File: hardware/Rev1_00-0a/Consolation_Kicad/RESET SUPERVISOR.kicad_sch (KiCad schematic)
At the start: 28 parts, among them Q7 SSM3K56FS,LF, Q8 SSM3K56FS,LF, Q9 SSM3K56FS,LF, U30 STM6710DWB6F, U31 SN74LVC1G125DBVR, U32 SN74HCS365QPWRQ1

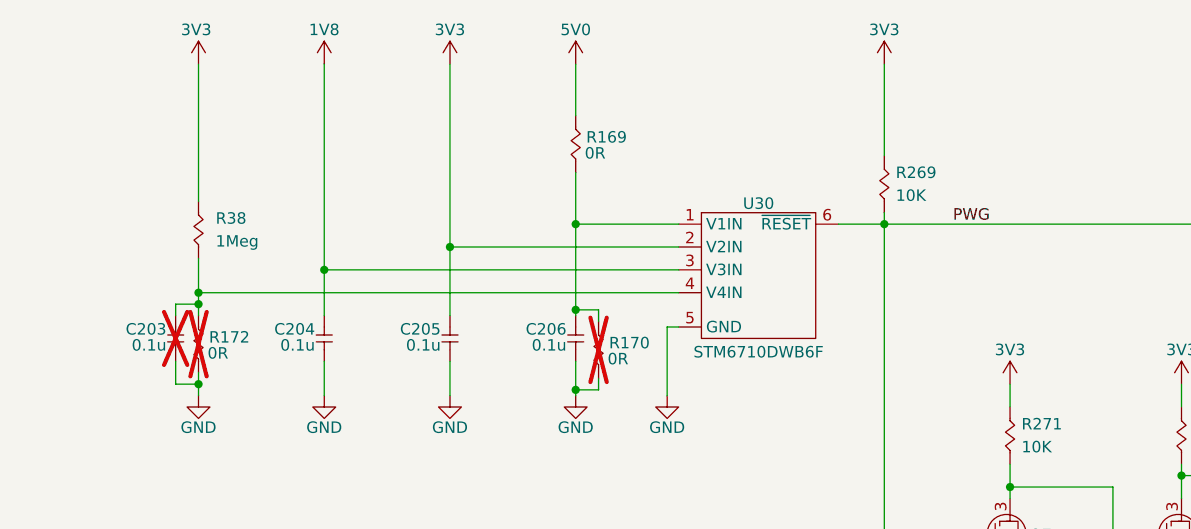
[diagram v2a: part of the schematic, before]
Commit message: Component preliminary placement
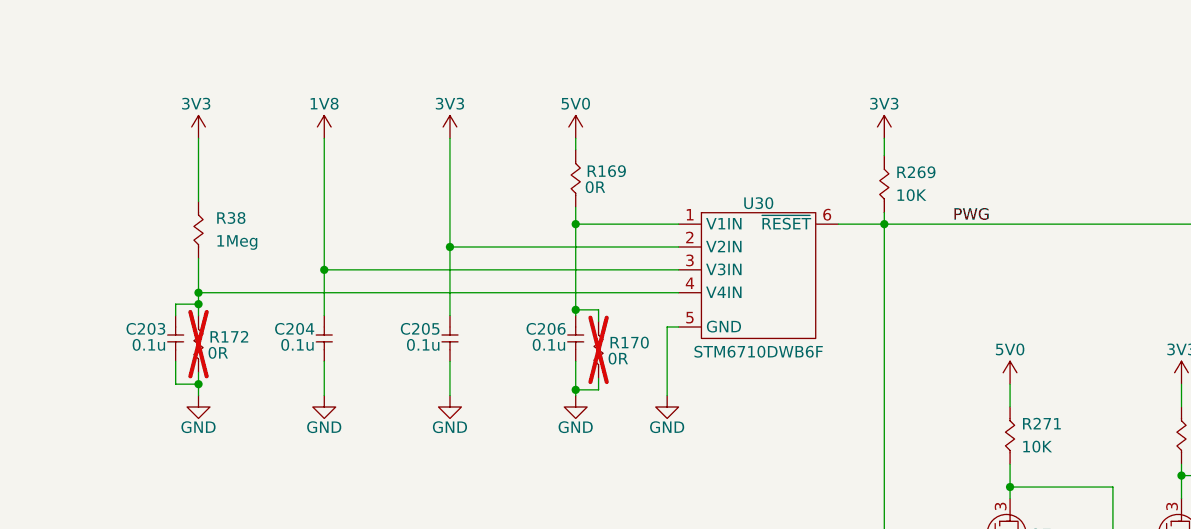
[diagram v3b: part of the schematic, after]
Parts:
- C203: now fitted
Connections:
- net 3V3: no longer R271.2
- net 5V0: now also R271.2
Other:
- moved on the sheet: R169
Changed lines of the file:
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@@
 	)
 	(junction
-		(at 78.105 64.77)
-		(diameter 0)
-		(color 0 0 0 0)
-	)
-	(junction
 		(at 209.55 107.95)
 		(diameter 0)
@@
 	)
 	(junction
-		(at 92.075 62.23)
+		(at 64.135 67.31)
 		(diameter 0)
 		(color 0 0 0 0)
@@
 	)
 	(junction
-		(at 64.135 67.31)
+		(at 78.105 64.77)
+		(diameter 0)
+		(color 0 0 0 0)
+	)
+	(junction
+		(at 92.075 62.23)
 		(diameter 0)
 		(color 0 0 0 0)
@@
 	(wire
 		(pts
-			(xy 50.165 44.45) (xy 50.165 59.69)
+			(xy 50.165 52.705) (xy 50.165 59.69)
 		)
 		(stroke
@@
 	(wire
 		(pts
-			(xy 78.105 44.45) (xy 78.105 64.77)
+			(xy 78.105 52.705) (xy 78.105 64.77)
 		)
 		(stroke
@@
 	(wire
 		(pts
-			(xy 92.075 56.515) (xy 92.075 62.23)
+			(xy 92.075 60.325) (xy 92.075 62.23)
 		)
 		(stroke
@@
 	(wire
 		(pts
-			(xy 126.365 44.45) (xy 126.365 54.61)
+			(xy 126.365 52.705) (xy 126.365 54.61)
 		)
 		(stroke
@@
 	(wire
 		(pts
+			(xy 64.135 67.31) (xy 64.135 72.39)
+		)
+		(stroke
+			(width 0)
+			(type default)
+		)
+	)
+	(wire
+		(pts
 			(xy 207.645 100.33) (xy 216.535 100.33)
 		)
@@
 	(wire
 		(pts
-			(xy 92.075 44.45) (xy 92.075 50.165)
+			(xy 92.075 52.705) (xy 92.075 53.975)
 		)
 		(stroke
@@
 	(wire
 		(pts
-			(xy 64.135 67.31) (xy 64.135 72.39)
-		)
-		(stroke
-			(width 0)
-			(type default)
-		)
-	)
-	(wire
-		(pts
 			(xy 235.585 62.23) (xy 235.585 63.5)
 		)
@@
 	(wire
 		(pts
-			(xy 64.135 44.45) (xy 64.135 67.31)
+			(xy 64.135 52.705) (xy 64.135 67.31)
 		)
 		(stroke
@@
 	(symbol
 		(lib_id "KiCad_Pwr_Symbols:+1V8")
-		(at 50.165 44.45 0)
+		(at 50.165 52.705 0)
 		(unit 1)
 		(body_style 1)
@@
 		(dnp no)
 		(property "Reference" "#PWR0300"
-			(at 50.165 48.26 0)
+			(at 50.165 56.515 0)
 			(hide yes)
 			(show_name no)
@@
 		)
 		(property "Value" "3V3"
-			(at 49.911 40.64 0)
+			(at 49.911 48.895 0)
 			(show_name no)
 			(do_not_autoplace no)
@@
 		)
 		(property "Footprint" ""
-			(at 50.165 44.45 0)
+			(at 50.165 52.705 0)
 			(hide yes)
 			(show_name no)
@@
 		)
 		(property "Datasheet" ""
-			(at 50.165 44.45 0)
+			(at 50.165 52.705 0)
 			(hide yes)
 			(show_name no)
@@
 		)
 		(property "Description" "Power symbol creates a global label with name \"+1V8\""
-			(at 50.165 44.45 0)
+			(at 50.165 52.705 0)
 			(hide yes)
 			(show_name no)
@@
 	(symbol
 		(lib_id "KiCad_Pwr_Symbols:+1V8")
-		(at 78.105 44.45 0)
+		(at 78.105 52.705 0)
 		(unit 1)
 		(body_style 1)
@@
 		(dnp no)
 		(property "Reference" "#PWR0304"
-			(at 78.105 48.26 0)
+			(at 78.105 56.515 0)
 			(hide yes)
 			(show_name no)
@@
 		)
 		(property "Value" "3V3"
-			(at 78.105 40.64 0)
+			(at 78.105 48.895 0)
 			(show_name no)
 			(do_not_autoplace no)
@@
 		)
 		(property "Footprint" ""
-			(at 78.105 44.45 0)
+			(at 78.105 52.705 0)
 			(hide yes)
 			(show_name no)
@@
 		)
 		(property "Datasheet" ""
-			(at 78.105 44.45 0)
+			(at 78.105 52.705 0)
 			(hide yes)
 			(show_name no)
@@
 		)
 		(property "Description" "Power symbol creates a global label with name \"+1V8\""
-			(at 78.105 44.45 0)
+			(at 78.105 52.705 0)
 			(hide yes)
 			(show_name no)
@@
 			)
 		)
-		(property "Value" "3V3"
+		(property "Value" "5V0"
 			(at 140.335 76.2 0)
 			(show_name no)
@@
 	(symbol
 		(lib_id "KicadCompDb:Resistors/RES_SMT_00001")
-		(at 92.075 55.245 90)
+		(at 92.075 59.055 90)
 		(unit 1)
 		(body_style 1)
@@
 		(dnp no)
 		(property "Reference" "R169"
-			(at 95.504 52.578 90)
+			(at 95.504 56.388 90)
 			(show_name no)
 			(do_not_autoplace no)
@@
 		)
 		(property "Value" "0R"
-			(at 94.234 54.356 90)
+			(at 94.234 58.166 90)
 			(show_name no)
 			(do_not_autoplace no)
@@
 		)
 		(property "Footprint" "footprint:RES_0402"
-			(at 114.173 54.737 0)
+			(at 114.173 58.547 0)
 			(hide yes)
 			(show_name no)
@@
 		)
 		(property "Datasheet" "https://www.yageogroup.com/content/datasheet/asset/file/PYU-RC_GROUP_51_ROHS_L"
-			(at 92.075 55.245 0)
+			(at 92.075 59.055 0)
 			(hide yes)
 			(show_name no)
@@
 		)
 		(property "Description" "RES 0 OHM JUMPER 1/16W 0402"
-			(at 101.981 53.467 0)
+			(at 101.981 57.277 0)
 			(hide yes)
 			(show_name no)
@@
 		)
 		(property "Tolerance" "1%"
-			(at 112.395 54.991 0)
+			(at 112.395 58.801 0)
 			(hide yes)
 			(show_name no)
@@
 		)
 		(property "Power" "1/16W"
-			(at 106.299 54.991 0)
+			(at 106.299 58.801 0)
 			(hide yes)
 			(show_name no)
@@
 		)
 		(property "Package" "0402"
-			(at 108.331 55.245 0)
+			(at 108.331 59.055 0)
 			(hide yes)
 			(show_name no)
@@
 		)
 		(property "Manufacturer" "YAGEO"
-			(at 110.363 54.991 0)
+			(at 110.363 58.801 0)
 			(hide yes)
 			(show_name no)
@@
 		)
 		(property "Manufacturer Part Number" "RC0402FR-071KL"
-			(at 99.949 54.991 0)
+			(at 99.949 58.801 0)
 			(hide yes)
 			(show_name no)
@@
 		)
 		(property "Distributor" "DigiKey"
-			(at 97.917 55.245 0)
+			(at 97.917 59.055 0)
 			(hide yes)
 			(show_name no)
@@
 		)
 		(property "Distributor Part Number" "311-0.0JRCT-ND"
-			(at 104.267 54.483 0)
+			(at 104.267 58.293 0)
 			(hide yes)
 			(show_name no)
@@
 		)
 		(property "Temperature Coefficient" "±100ppm/°C"
-			(at 92.075 55.245 0)
+			(at 92.075 59.055 0)
 			(hide yes)
 			(show_name no)
@@
 		)
 		(property "Operating Temperature" "-55°C ~ 155°C"
-			(at 116.459 54.483 0)
+			(at 116.459 58.293 0)
 			(hide yes)
 			(show_name no)
@@
 		)
 		(property "Type" "RES SMT"
-			(at 92.075 55.245 0)
+			(at 92.075 59.055 0)
 			(hide yes)
 			(show_name yes)
@@
 		)
 		(property "Dimensions" "1.00mm x 0.50mm"
-			(at 92.075 55.245 0)
+			(at 92.075 59.055 0)
 			(hide yes)
 			(show_name yes)
@@
 	(symbol
 		(lib_id "KiCad_Pwr_Symbols:+1V8")
-		(at 126.365 44.45 0)
+		(at 126.365 52.705 0)
 		(unit 1)
 		(body_style 1)
@@
 		(dnp no)
 		(property "Reference" "#PWR0318"
-			(at 126.365 48.26 0)
+			(at 126.365 56.515 0)
 			(hide yes)
 			(show_name no)
@@
 		)
 		(property "Value" "3V3"
-			(at 126.365 40.64 0)
+			(at 126.365 48.895 0)
 			(show_name no)
 			(do_not_autoplace no)
@@
 		)
 		(property "Footprint" ""
-			(at 126.365 44.45 0)
+			(at 126.365 52.705 0)
 			(hide yes)
 			(show_name no)
@@
 		)
 		(property "Datasheet" ""
-			(at 126.365 44.45 0)
+			(at 126.365 52.705 0)
 			(hide yes)
 			(show_name no)
@@
 		)
 		(property "Description" "Power symbol creates a global label with name \"+1V8\""
-			(at 126.365 44.45 0)
+			(at 126.365 52.705 0)
 			(hide yes)
 			(show_name no)
@@
 		(on_board yes)
 		(in_pos_files yes)
-		(dnp yes)
+		(dnp no)
 		(property "Reference" "C203"
 			(at 46.609 73.914 90)
@@
 	(symbol
 		(lib_id "KiCad_Pwr_Symbols:+1V8")
-		(at 64.135 44.45 0)
+		(at 64.135 52.705 0)
 		(unit 1)
 		(body_style 1)
@@
 		(dnp no)
 		(property "Reference" "#PWR0302"
-			(at 64.135 48.26 0)
+			(at 64.135 56.515 0)
 			(hide yes)
 			(show_name no)
@@
 		)
 		(property "Value" "1V8"
-			(at 64.135 40.64 0)
+			(at 64.135 48.895 0)
 			(show_name no)
 			(do_not_autoplace no)
@@
 		)
 		(property "Footprint" ""
-			(at 64.135 44.45 0)
+			(at 64.135 52.705 0)
 			(hide yes)
 			(show_name no)
@@
 		)
 		(property "Datasheet" ""
-			(at 64.135 44.45 0)
+			(at 64.135 52.705 0)
 			(hide yes)
 			(show_name no)
@@
 		)
 		(property "Description" "Power symbol creates a global label with name \"+1V8\""
-			(at 64.135 44.45 0)
+			(at 64.135 52.705 0)
 			(hide yes)
 			(show_name no)
@@
 	(symbol
 		(lib_id "KiCad_Pwr_Symbols:+1V8")
-		(at 92.075 44.45 0)
+		(at 92.075 52.705 0)
 		(unit 1)
 		(body_style 1)
@@
 		(dnp no)
 		(property "Reference" "#PWR0307"
-			(at 92.075 48.26 0)
+			(at 92.075 56.515 0)
 			(hide yes)
 			(show_name no)
@@
 		)
 		(property "Value" "5V0"
-			(at 92.075 40.64 0)
+			(at 92.075 48.895 0)
 			(show_name no)
 			(do_not_autoplace no)
@@
 		)
 		(property "Footprint" ""
-			(at 92.075 44.45 0)
+			(at 92.075 52.705 0)
 			(hide yes)
 			(show_name no)
@@
 		)
 		(property "Datasheet" ""
-			(at 92.075 44.45 0)
+			(at 92.075 52.705 0)
 			(hide yes)
 			(show_name no)
@@
 		)
 		(property "Description" "Power symbol creates a global label with name \"+1V8\""
-			(at 92.075 44.45 0)
+			(at 92.075 52.705 0)
 			(hide yes)
 			(show_name no)

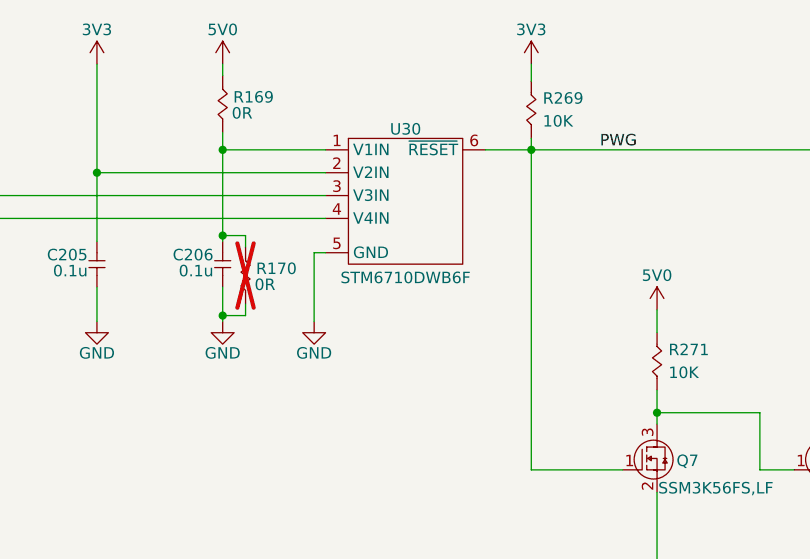
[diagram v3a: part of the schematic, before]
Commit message: Update ConJoy L2 trigger (2-level trigger instead) Update ConJoy all output files accordingly
Work on Consolation preliminary placement
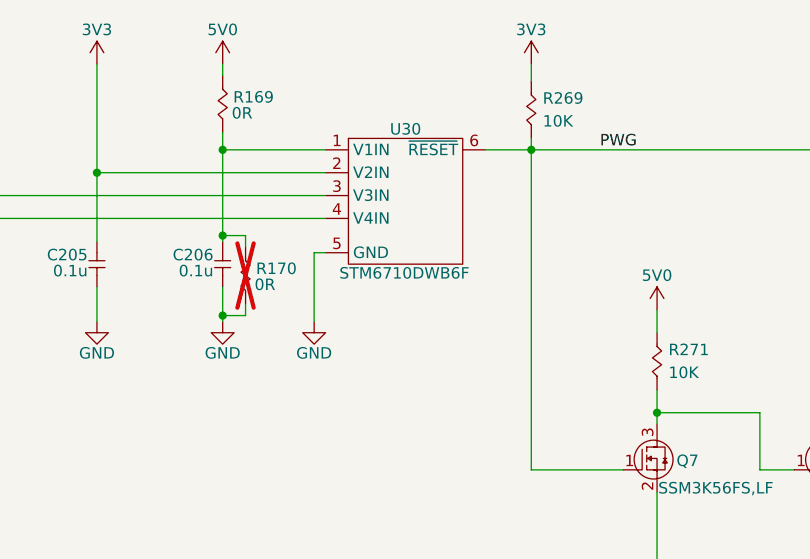
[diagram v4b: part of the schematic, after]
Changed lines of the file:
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@@
 	(title_block
 		(title "Consolation [Console Emulation]")
-		(date "2026-08-08")
+		(date "2026-08-23")
 		(rev "1.00-0A")
 		(comment 1 "Jean-Francois Bilodeau")
@@
 		)
 		(property "Value" "STM6710DWB6F"
-			(at 112.395 76.454 0)
+			(at 112.268 75.946 0)
 			(show_name no)
 			(do_not_autoplace no)

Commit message: Continue preliminary placement To do : Power supplies + Type C charger
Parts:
- added R205: 6K04, footprint:RES_0402, symbol KicadCompDb:Resistors/RES_SMT_00011
- added R206, R207, R214, R215: 0R, footprint:RES_0402, symbol KicadCompDb:Resistors/RES_SMT_00001
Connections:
- net 1V8: now also R207.2; no longer C204.2, U30.3 (V3IN)
- net 3V3: now also R206.2; no longer C205.2, R272.2, U30.2 (V2IN)
- net 5V0: now also R205.1
- net GND: now also R272.1, R214.1, R215.1
- net at Q8.3 (D), U32.10 (A4), U32.12 (A5)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: now also R272.2, R205.2; no longer R272.1
- new net: C204.2, R207.1, R215.2, U30.3 (V3IN)
- new net: C205.2, R206.1, R214.2, U30.2 (V2IN)
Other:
- moved on the sheet: C203, R172, R38

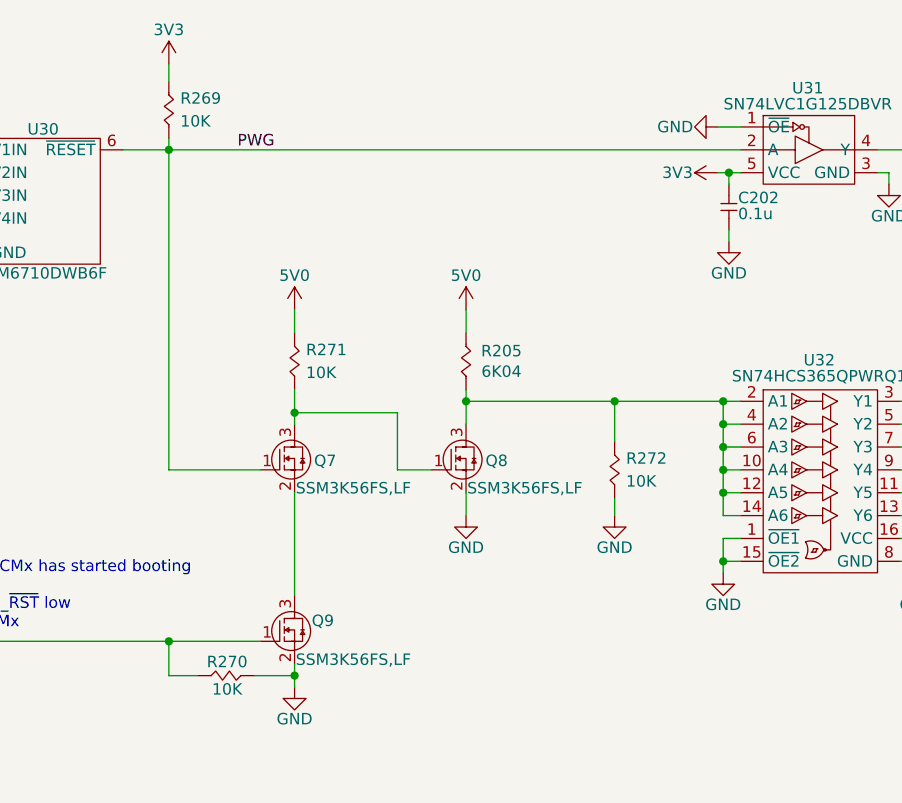
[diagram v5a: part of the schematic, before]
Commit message: Preliminary placement done Add test points to PCB
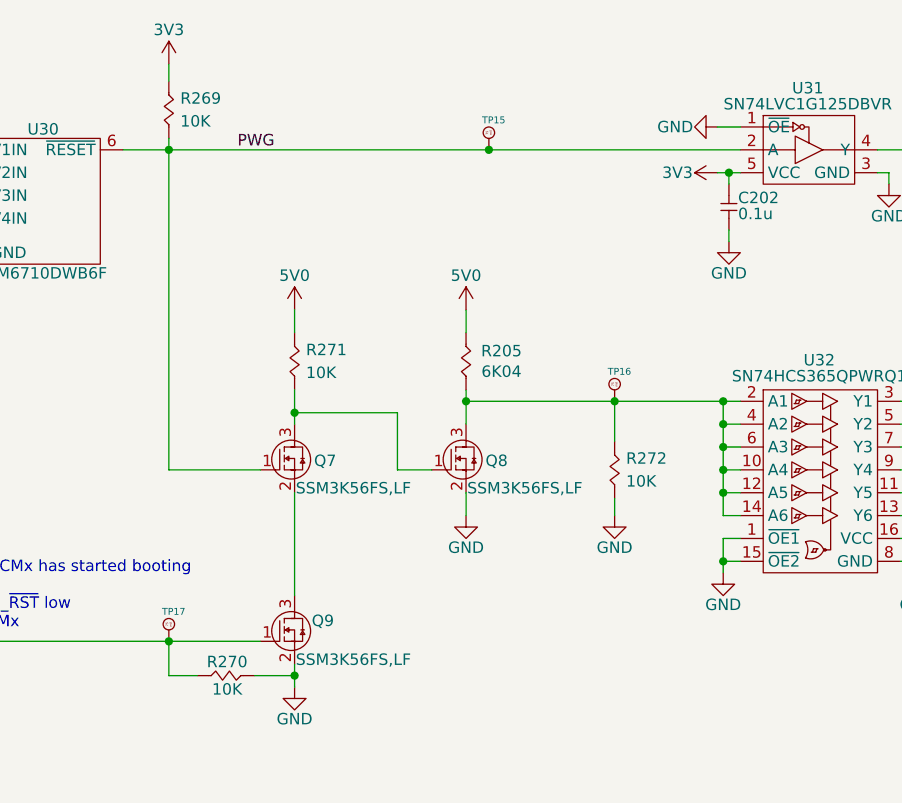
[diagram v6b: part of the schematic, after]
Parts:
- added TP15, TP16, TP17: 75 mils, footprint:SMT_TP_75_MILS, symbol KicadCompDb:Test Point/TP_00004
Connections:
- net EXT_~{RST}: now also TP17.1
- net PWG: now also TP15.1
- net at Q8.3 (D), R205.2, R272.2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: now also TP16.1

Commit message: Preliminary routing (DiffPairs, Power planes) in progress Slight changes to schematics to accommodate routing
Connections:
- net ~{BAT_CHRG_RST}: now also R90.2; no longer R122.2
- net ~{CODEC_RST}: now also R122.2; no longer R307.2
- net ~{DSI_BRDG_RST}: now also R123.2; no longer R282.2
- net ~{RP2350_RST}: now also R282.2; no longer R123.2
- net ~{TFT_RST}: now also R307.2; no longer R90.2
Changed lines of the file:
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@@
 	(title_block
 		(title "Consolation [Console Emulation]")
-		(date "2026-09-20")
+		(date "2026-10-12")
 		(rev "1.00-0A")
 		(comment 1 "Jean-Francois Bilodeau")
@@
 		)
 	)
-	(hierarchical_label "~{TFT_RST}"
+	(hierarchical_label "~{DSI_BRDG_RST}"
 		(shape output)
-		(at 229.235 92.71 0)
+		(at 229.235 97.79 0)
 		(effects
 			(font
@@
 	(hierarchical_label "~{RP2350_RST}"
 		(shape output)
-		(at 229.235 97.79 0)
+		(at 229.235 90.17 0)
 		(effects
 			(font
@@
 		)
 	)
-	(hierarchical_label "~{DSI_BRDG_RST}"
-		(shape output)
-		(at 229.235 90.17 0)
-		(effects
-			(font
-				(size 1.27 1.27)
-			)
-			(justify left)
-		)
-	)
 	(hierarchical_label "~{HDMI_RST}"
 		(shape output)
@@
 	(hierarchical_label "~{BAT_CHRG_RST}"
 		(shape output)
-		(at 229.235 95.25 0)
+		(at 229.235 92.71 0)
 		(effects
 			(font
@@
 		)
 	)
+	(hierarchical_label "~{TFT_RST}"
+		(shape output)
+		(at 229.235 100.33 0)
+		(effects
+			(font
+				(size 1.27 1.27)
+			)
+			(justify left)
+		)
+	)
 	(hierarchical_label "~{CODEC_RST}"
 		(shape output)
-		(at 229.235 100.33 0)
+		(at 229.235 95.25 0)
 		(effects
 			(font
@@
 			(justify left bottom)
 		)
-		(property "Net Class" "CRITICAL"
+		(property "Netclass" "CRITICAL"
 			(at 146.1135 59.69 0)
 			(show_name no)
